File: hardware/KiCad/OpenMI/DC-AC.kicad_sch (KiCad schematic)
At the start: 35 parts, among them Q2 IPL60R125P7, Q3 IPL60R125P7, U1 IRS2304S

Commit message: feat(hw): Adds filter capacitor
build(hw): Synchronize parts
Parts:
- removed C? (x3): 30uF_450V, OpenCE:C_Rect_L43mm_W42mm_H25mm_P37.5mm_P20.3mm_KEMET, symbol _C_Film:30uF_450V
- removed C?: C, symbol Device:C
- added C1, C2, C3: 30u_600V, OpenCE:C_Rect_L43mm_W42mm_H25mm_P37.5mm_P20.3mm_KEMET, symbol _C_Film:30u_600V
- added C7: 470n_630V, Capacitor_THT:C_Rect_L18.0mm_W8.0mm_P15.00mm_FKS3_FKP3, symbol _C_Film:470n_630V
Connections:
- net GND: now also C1.2, C2.2, C3.2
- net INV_{2}: now also C7.2
- net VBUS: now also C1.1, C2.1, C3.1
- net at L?.1, L?.2: now also C7.1

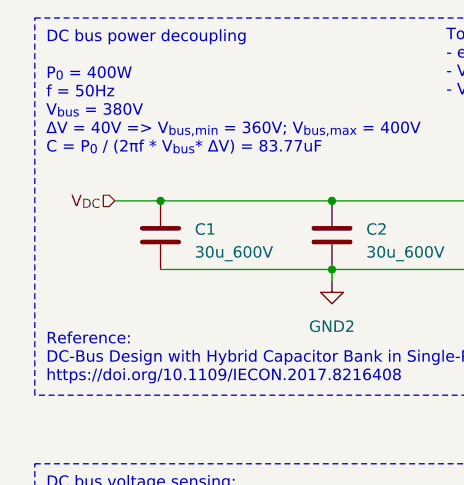
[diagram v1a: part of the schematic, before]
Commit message: refactor(hw): Rename hierarchical label V_DC -> V_BUS
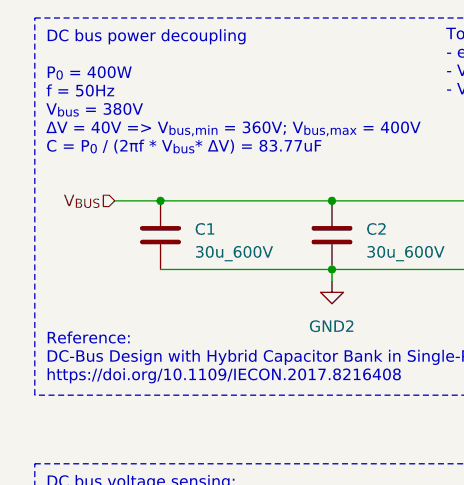
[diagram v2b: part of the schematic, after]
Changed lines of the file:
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@@
     (effects (font (size 1.27 1.27)) (justify right))
   )
-  (hierarchical_label "V_{DC}" (shape input) (at 25.4 36.83 180) (fields_autoplaced)
+  (hierarchical_label "V_{BUS}" (shape input) (at 25.4 36.83 180) (fields_autoplaced)
     (effects (font (size 1.27 1.27)) (justify right))
   )

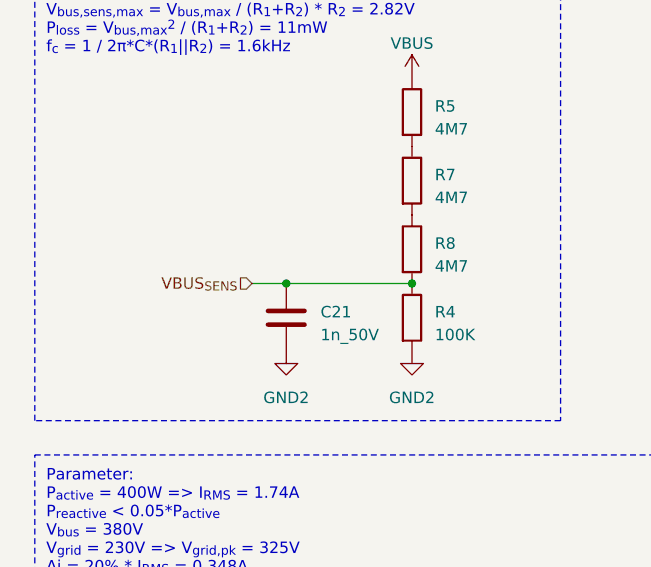
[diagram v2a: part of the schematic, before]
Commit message: fix(hw): Fix hierarchical label direction
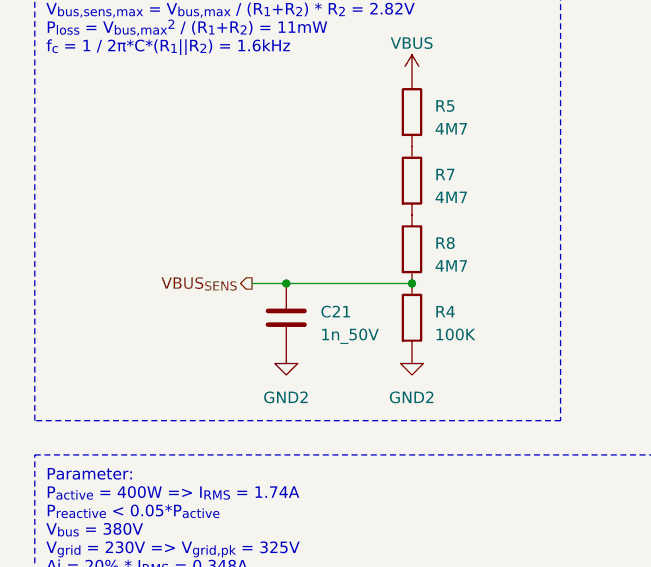
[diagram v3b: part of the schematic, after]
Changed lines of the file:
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@@
     (effects (font (size 1.27 1.27)) (justify right))
   )
-  (hierarchical_label "VBUS_{SENS}" (shape input) (at 40.64 106.68 180) (fields_autoplaced)
+  (hierarchical_label "VBUS_{SENS}" (shape output) (at 40.64 106.68 180) (fields_autoplaced)
     (effects (font (size 1.27 1.27)) (justify right))
   )

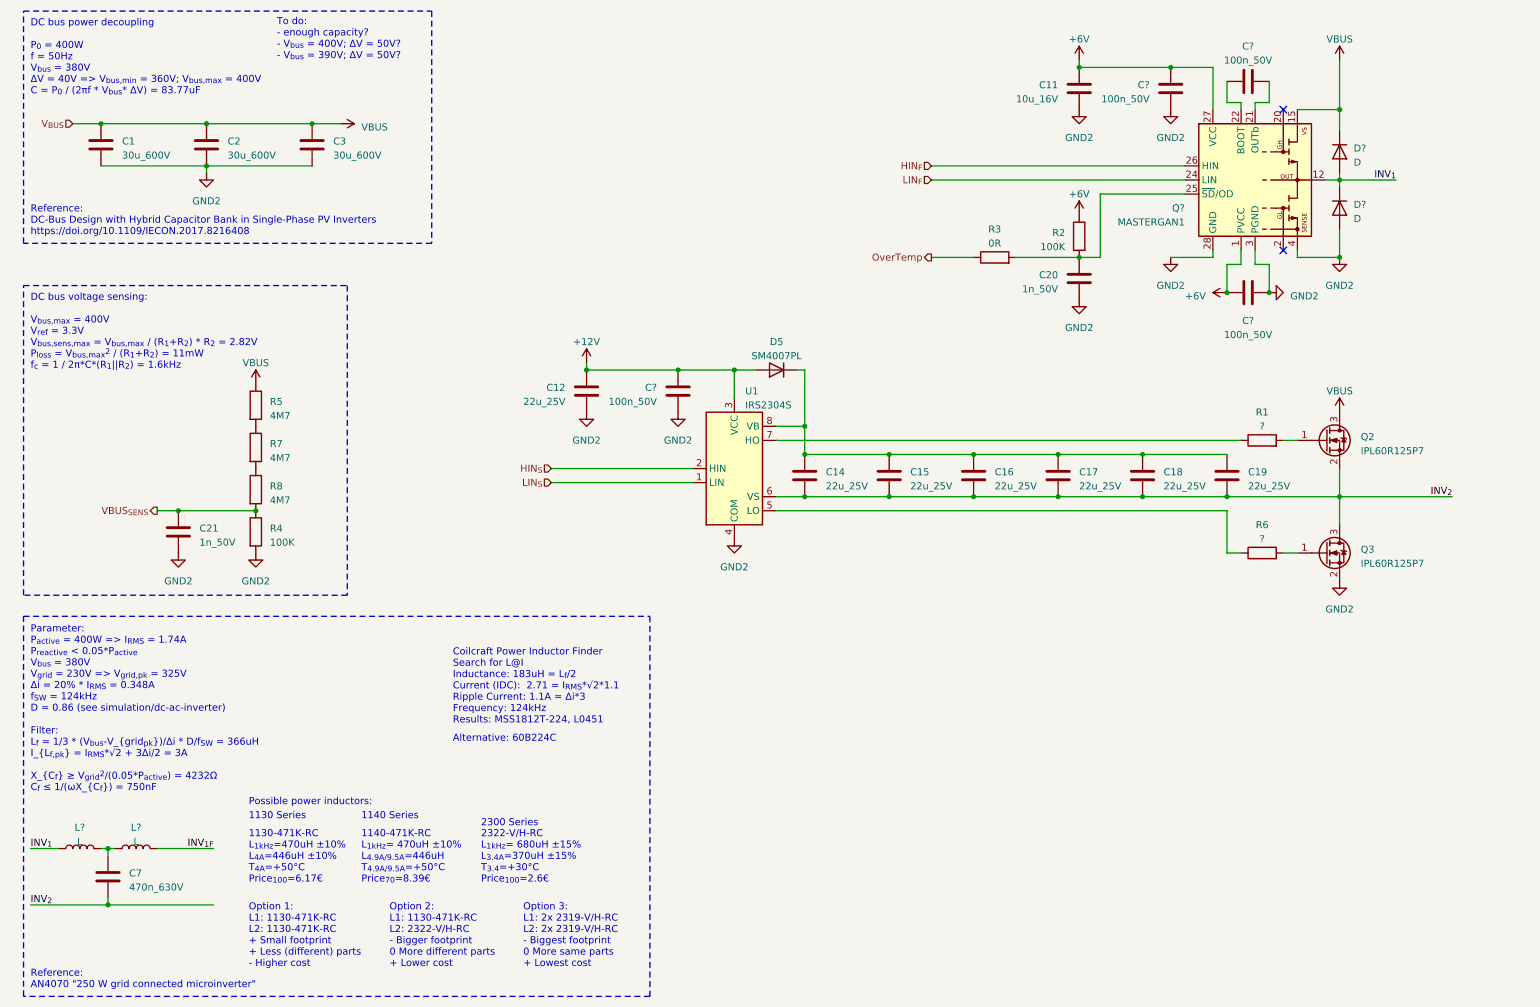
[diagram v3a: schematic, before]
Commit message: refactor(hw): rearrange DC-AC schematic
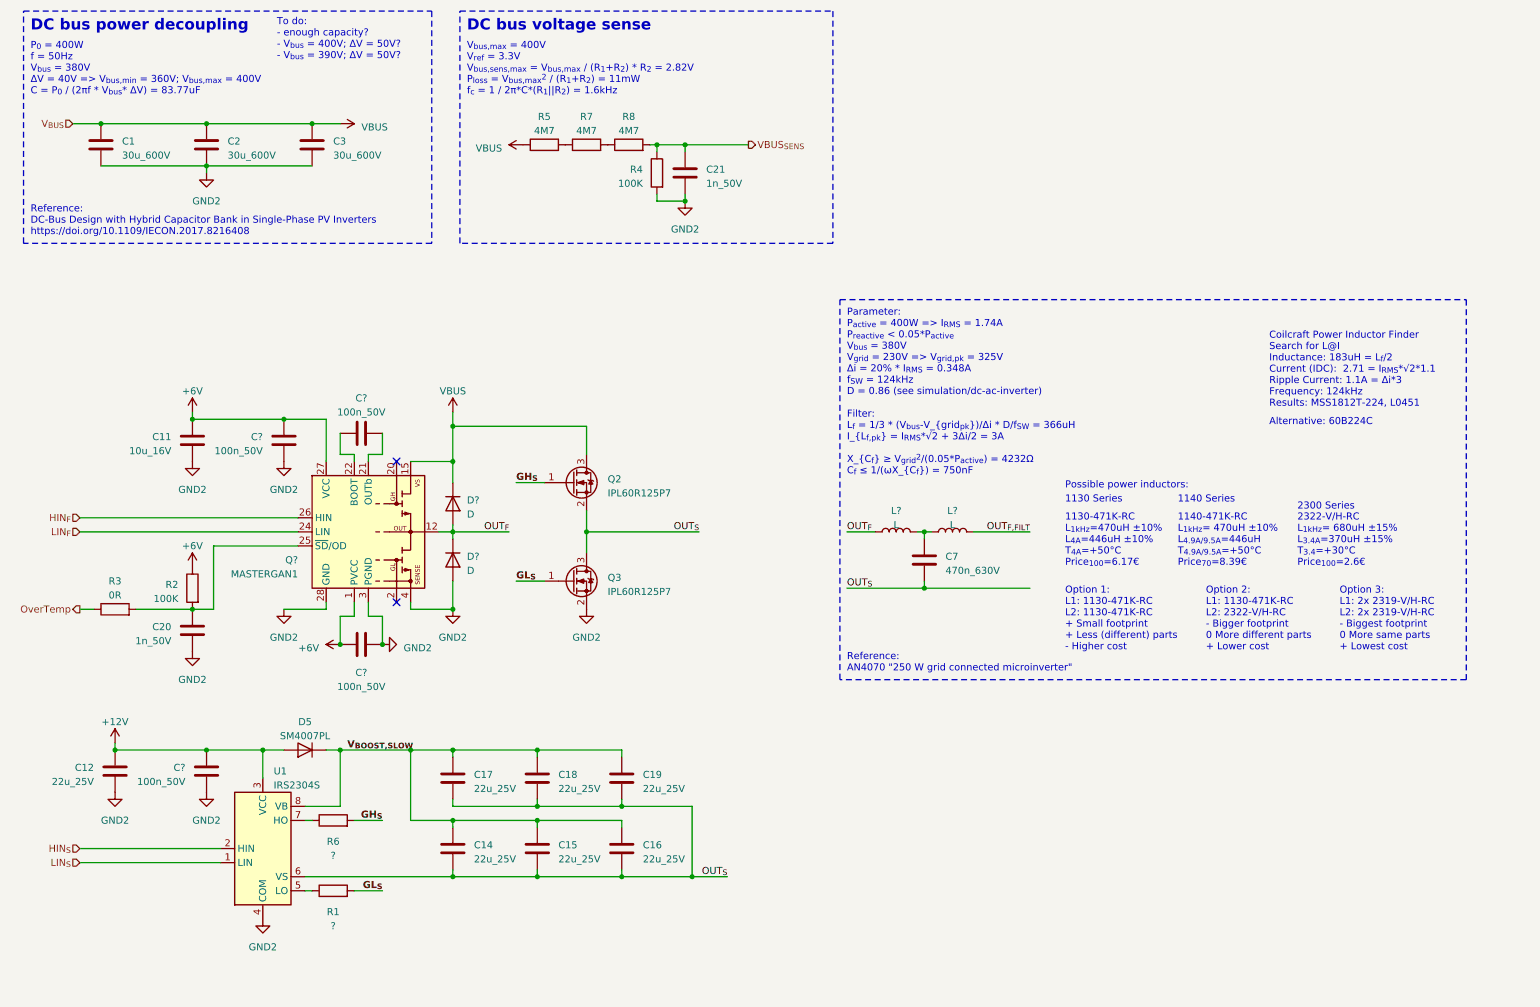
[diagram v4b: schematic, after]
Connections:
- net GH_{S}: now reaches R6.2
- net GH_{S}: now also Q2.1 (G); no longer Q3.1 (G)
- net V_{BOOST,SLOW}: now reaches C14.1, C15.1, C16.1, C17.1, C18.1, C19.1, D5.1 (K), U1.8 (VB)
- net GL_{S}: now reaches R1.2
- net GL_{S}: now also Q3.1 (G); no longer Q2.1 (G)
- net at R1.1: now also U1.5 (LO); no longer U1.7 (HO)
- net at R6.1: now also U1.7 (HO); no longer U1.5 (LO)
- net INV_{1F} renamed OUT_{F,FILT}
- net INV_{1} renamed OUT_{F}
- net INV_{2} renamed OUT_{S}
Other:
- note added: "DC bus power decoupling"
- note added: "DC bus voltage sense"
- note added: "P_{0} = 400W f = 50Hz V_{bus} = 380V ΔV = 40V => V_{bus,min} = 360V; V_{bus,max} = 400V C = P_{0} / (2πf * V_{bus}* ΔV) = 83.77uF"
- note added: "V_{bus,max} = 400V V_{ref} = 3.3V V_{bus,sens,max} = V_{bus,max} / (R_{1}+R_{2}) * R_{2} = 2.82V P_{loss} = V_{bus,max}^{2} / (R_{1}+R_{2}) = 11mW f_{c} = 1 / 2π*C*(R_{1}||R_{2}) = 1.6kHz"
- note removed: "DC bus power decoupling P_{0} = 400W f = 50Hz V_{bus} = 380V ΔV = 40V => V_{bus,min} = 360V; V_{bus,max} = 400V C = P_{0} / (2πf * V_{bus}* ΔV) = 83.77uF"
- note removed: "DC bus voltage sensing: V_{bus,max} = 400V V_{ref} = 3.3V V_{bus,sens,max} = V_{bus,max} / (R_{1}+R_{2}) * R_{2} = 2.82V P_{loss} = V_{bus,max}^{2} / (R_{1}+R_{2}) = 11mW f_{c} = 1 / 2π*C*(R_{1}||R_{2}) = 1.6kHz"
- moved on the sheet: C11, C12, C14, C15, C16, C17, C18, C19, C20, C21, C7, C?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

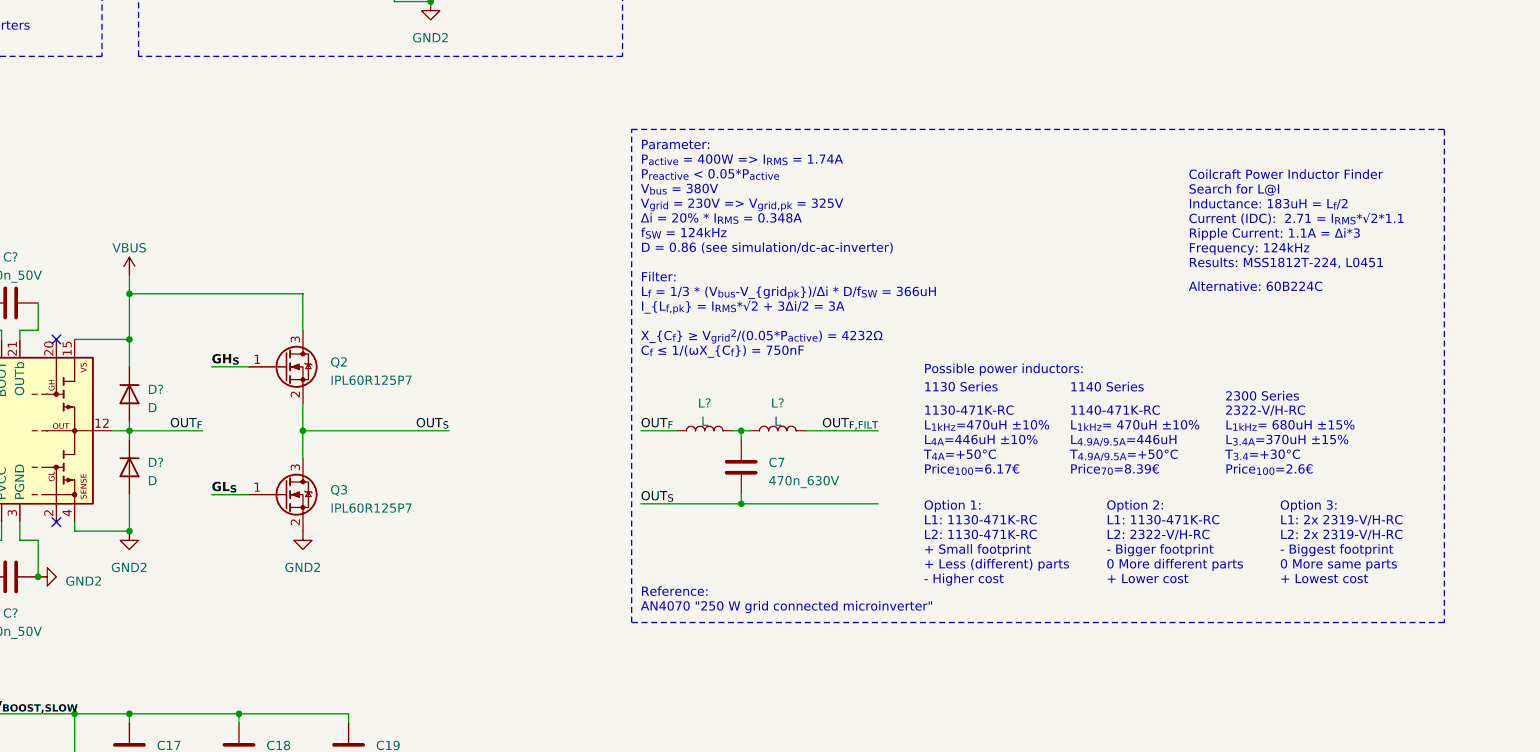
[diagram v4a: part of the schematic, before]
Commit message: feat: Adds grid-side filter inductance feat: Replaces outdated filter with placeholder capacitor and damping resistor feat: Adds resistors to gates of slow switching MOSFET to prevent accidental switching.
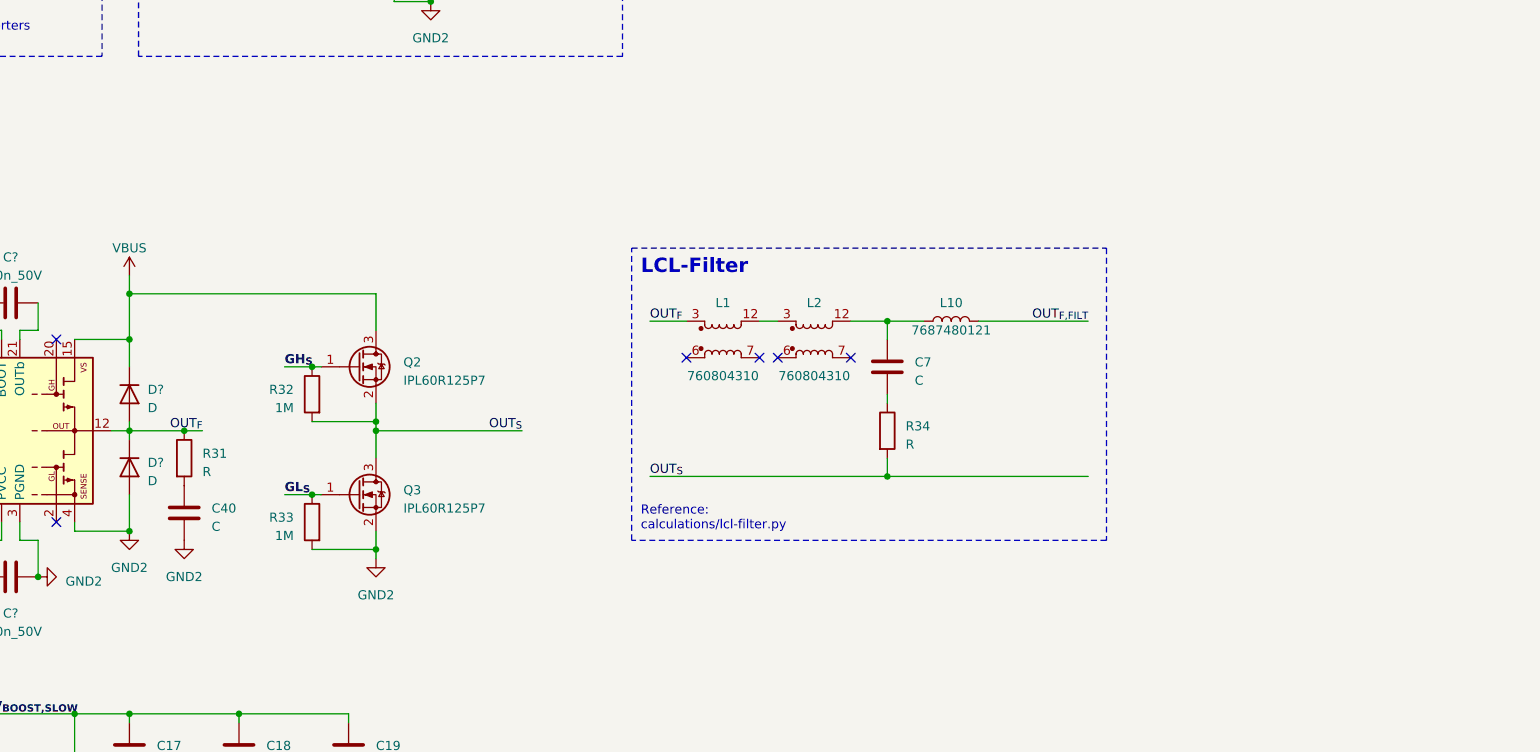
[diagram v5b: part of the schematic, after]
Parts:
- removed C7: 470n_630V, Capacitor_THT:C_Rect_L18.0mm_W8.0mm_P15.00mm_FKS3_FKP3, symbol _C_Film:470n_630V
- removed L? (x2): L, symbol Device:L
- added C40, C7: C, symbol Device:C
- added L1, L2: 760804310, OpenCE:WE-PFC_RM12, symbol _L_Power:760804310
- added L10: 7687480121, OpenCE:L_Radial_D10.5mm_P5.00mm_H14.5mm_Wuerth_1014, symbol _L_Power:7687480121
- added R31, R34: R, symbol Device:R
- added R32, R33: 1M, Resistor_SMD:R_0603_1608Metric, symbol _R_0603:1M
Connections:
- net GH_{S}: now also R32.1
- net GL_{S}: now also R33.1
- net GND: now also C40.2, R33.2
- net OUT_{F,FILT}: now also L10.2
- net OUT_{F}: now also L1.3, R31.1
- net OUT_{S}: now also R32.2, R34.2
- new net: C7.2, R34.1
- new net: C40.1, R31.2
- new net: C7.1, L10.1, L2.12
- new net: L1.12, L2.3
- no-connect marks 2 -> 6
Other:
- note added: "LCL-Filter"
- note added: "Reference: calculations/lcl-filter.py"
- note removed: "1130 Series"
- note removed: "1130-471K-RC L_{1kHz}=470uH ±10% L_{4A}=446uH ±10% T_{4A}=+50°C Price_{100}=6.17€"
- note removed: "1140 Series"
- note removed: "1140-471K-RC L_{1kHz}= 470uH ±10% L_{4.9A/9.5A}=446uH T_{4.9A/9.5A}=+50°C Price_{70}=8.39€"
- note removed: "2300 Series"
- note removed: "2322-V/H-RC L_{1kHz}= 680uH ±15% L_{3.4A}=370uH ±15% T_{3.4}=+30°C Price_{100}=2.6€"
- note removed: "Alternative: 60B224C"
- note removed: "Coilcraft Power Inductor Finder Search for L@I Inductance: 183uH = L_{f}/2 Current (IDC): 2.71 = I_{RMS}*√2*1.1 Ripple Current: 1.1A = Δi*3 Frequency: 124kHz Results: MSS1812T-224, L0451"
- note removed: "Option 1: L1: 1130-471K-RC L2: 1130-471K-RC + Small footprint + Less (different) parts - Higher cost"
- note removed: "Option 2: L1: 1130-471K-RC L2: 2322-V/H-RC - Bigger footprint 0 More different parts + Lower cost"
- note removed: "Option 3: L1: 2x 2319-V/H-RC L2: 2x 2319-V/H-RC - Biggest footprint 0 More same parts + Lowest cost"
- note removed: "Parameter: P_{active} = 400W => I_{RMS} = 1.74A P_{reactive} < 0.05*P_{active} V_{bus} = 380V V_{grid} = 230V => V_{grid,pk} = 325V Δi = 20% * I_{RMS} = 0.348A f_{SW} = 124kHz D = 0.86 (see simulation/dc-ac-inverter) Filter: L_{f} = 1/3 * (V_{bus}-V_{grid_{pk}})/Δi * D/f_{SW} = 366uH I_{L_{f,pk}} = I_{RMS}*√2 + 3Δi/2 = 3A X_{C_{f}} ≥ V_{grid}^{2}/(0.05*P_{active}) = 4232Ω C_{f} ≤ 1/(ωX_{C_{f}}) =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"
- note removed: "Possible power inductors:"
- note removed: "Reference: AN4070 "250 W grid connected microinverter""
- moved on the sheet: Q2, Q3
